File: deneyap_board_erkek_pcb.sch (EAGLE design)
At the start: 4 parts

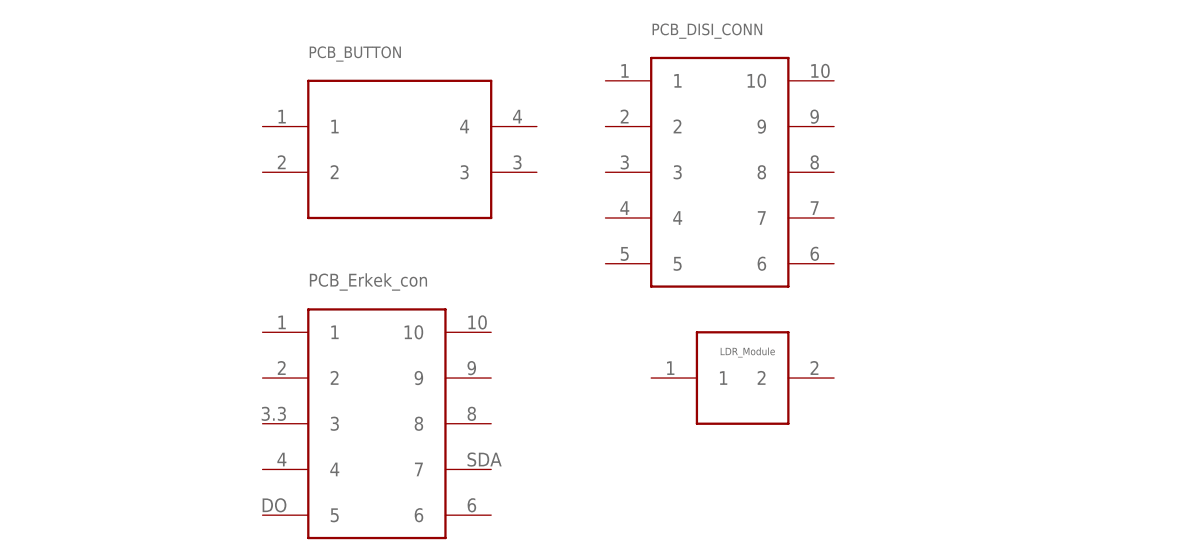
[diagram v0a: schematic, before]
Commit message: Update deneyap_board_erkek_pcb.sch
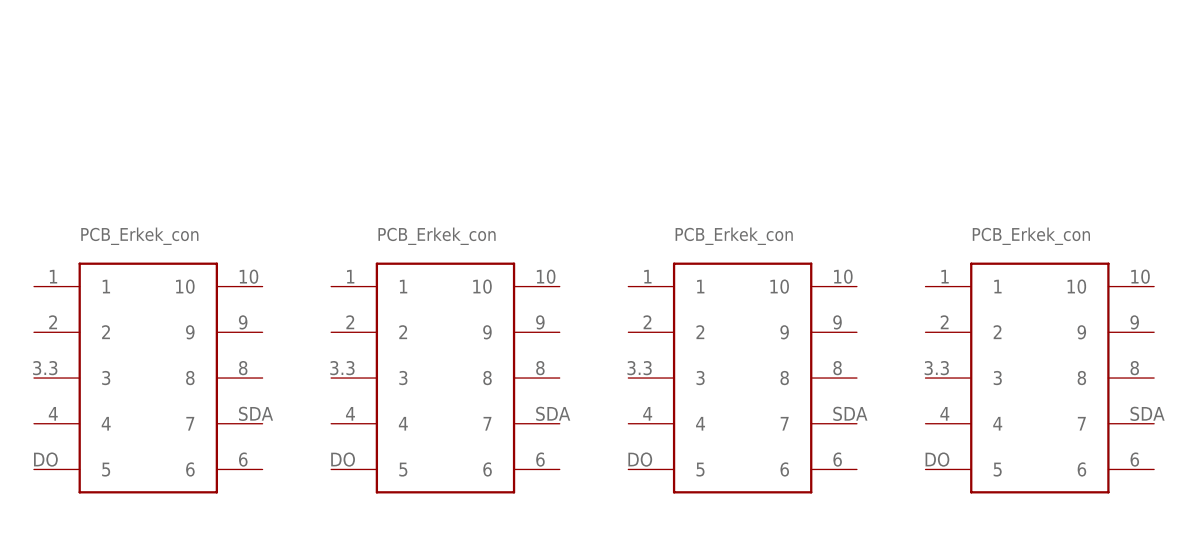
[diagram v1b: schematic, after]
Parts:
- U$1: value PCB_BUTTON_MODULE -> PCB_ERKEK_CONNECTORA; device deneyap_board_erkek_pcb_lib:PCB_BUTTON_MODULE -> deneyap_board_erkek_pcb_lib:PCB_ERKEK_CONNECTORA
- U$2: value PCB_DISI_CONNECTORA -> PCB_ERKEK_CONNECTORA; device deneyap_board_erkek_pcb_lib:PCB_DISI_CONNECTORA -> deneyap_board_erkek_pcb_lib:PCB_ERKEK_CONNECTORA
- U$4: value PCB_LDR_MODULE -> PCB_ERKEK_CONNECTORA; device deneyap_board_erkek_pcb_lib:PCB_LDR_MODULE -> deneyap_board_erkek_pcb_lib:PCB_ERKEK_CONNECTORA
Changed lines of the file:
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@@
 </classes>
 <parts>
-<part name="U$1" library="deneyap_board_erkek_pcb_lib" deviceset="PCB_BUTTON_MODULE" device=""/>
-<part name="U$2" library="deneyap_board_erkek_pcb_lib" deviceset="PCB_DISI_CONNECTOR" device="A"/>
+<part name="U$1" library="deneyap_board_erkek_pcb_lib" deviceset="PCB_ERKEK_CONNECTOR" device="A"/>
+<part name="U$2" library="deneyap_board_erkek_pcb_lib" deviceset="PCB_ERKEK_CONNECTOR" device="A"/>
 <part name="U$3" library="deneyap_board_erkek_pcb_lib" deviceset="PCB_ERKEK_CONNECTOR" device="A"/>
-<part name="U$4" library="deneyap_board_erkek_pcb_lib" deviceset="PCB_LDR_MODULE" device=""/>
+<part name="U$4" library="deneyap_board_erkek_pcb_lib" deviceset="PCB_ERKEK_CONNECTOR" device="A"/>
 </parts>
 <sheets>
@@
 </plain>
 <instances>
-<instance part="U$1" gate="G$1" x="33.02" y="76.2" smashed="yes"/>
-<instance part="U$2" gate="G$1" x="68.58" y="76.2" smashed="yes"/>
-<instance part="U$3" gate="G$1" x="30.48" y="48.26" smashed="yes"/>
-<instance part="U$4" gate="G$1" x="71.12" y="50.8" smashed="yes"/>
+<instance part="U$1" gate="G$1" x="5.08" y="53.34" smashed="yes"/>
+<instance part="U$2" gate="G$1" x="38.1" y="53.34" smashed="yes"/>
+<instance part="U$3" gate="G$1" x="71.12" y="53.34" smashed="yes"/>
+<instance part="U$4" gate="G$1" x="104.14" y="53.34" smashed="yes"/>
 </instances>
 <busses>
